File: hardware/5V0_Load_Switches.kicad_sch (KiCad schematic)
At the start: 28 parts, among them Q18 SI2302DDS-T1-GE3, Q19 SI2302DDS-T1-GE3, Q20 SI2302DDS-T1-GE3, U1 LMV321RIYLT, U10 INA199C3DCKR, U4 INA199C1DCKR, U5 NVTFS5116PLTAG, U6 NVTFS5116PLTAG, U7 NVTFS5116PLTAG, U9 INA199C3DCKR

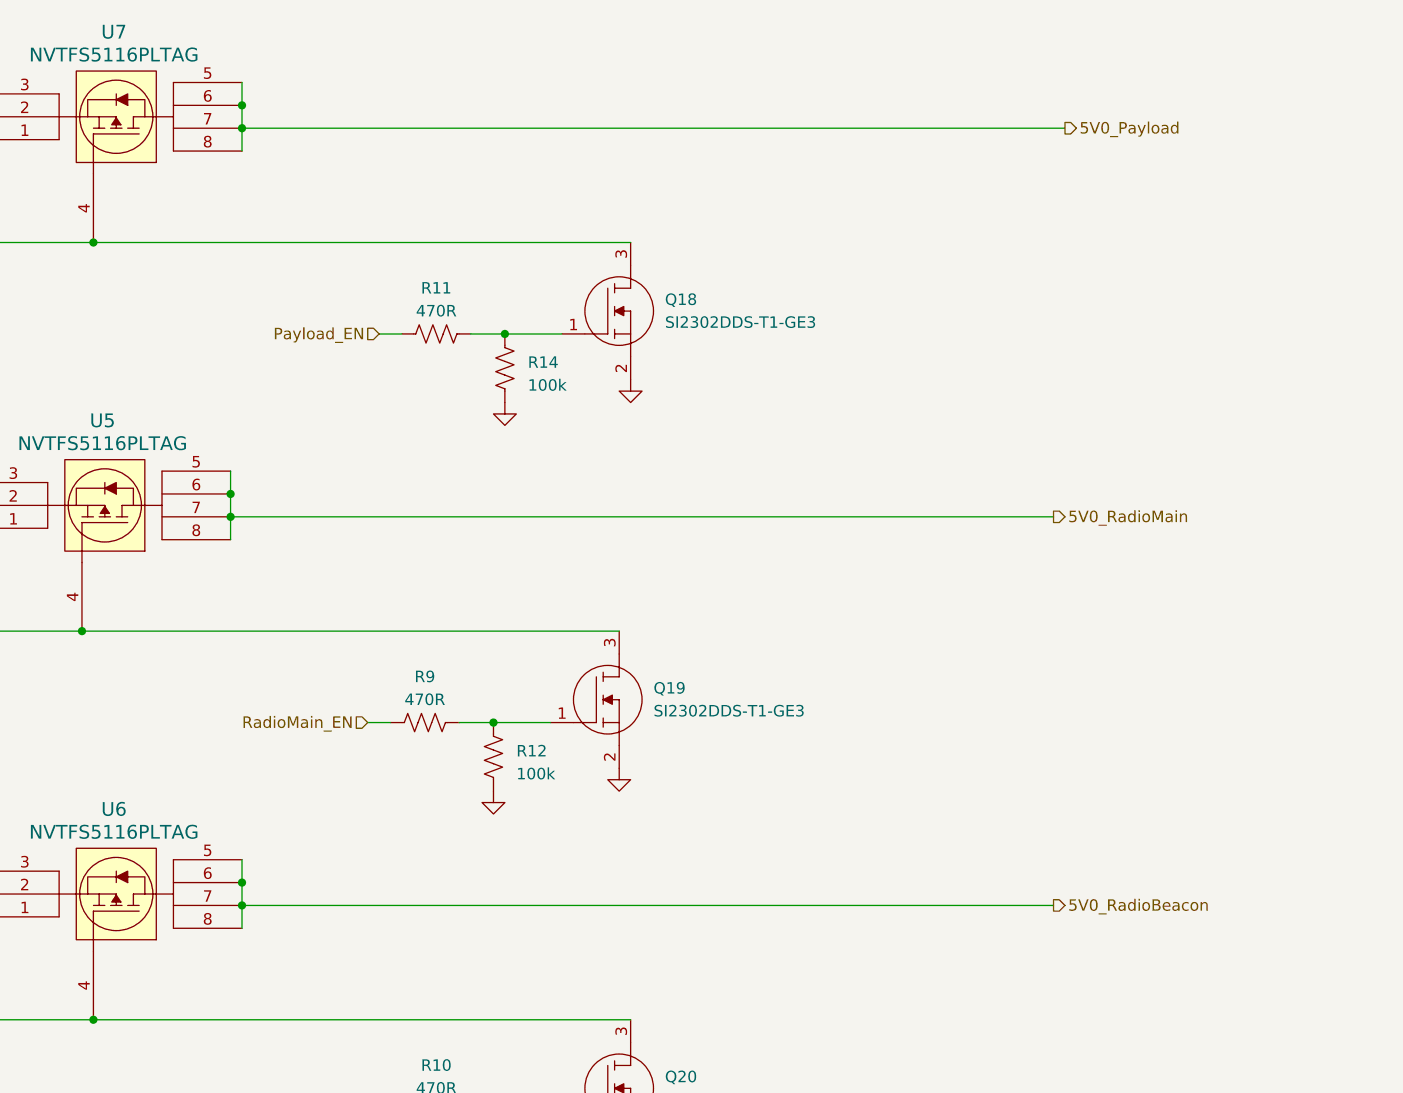
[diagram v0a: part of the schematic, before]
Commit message: hardware: Adding some 3D models, changing the placement of components and routing more nets.
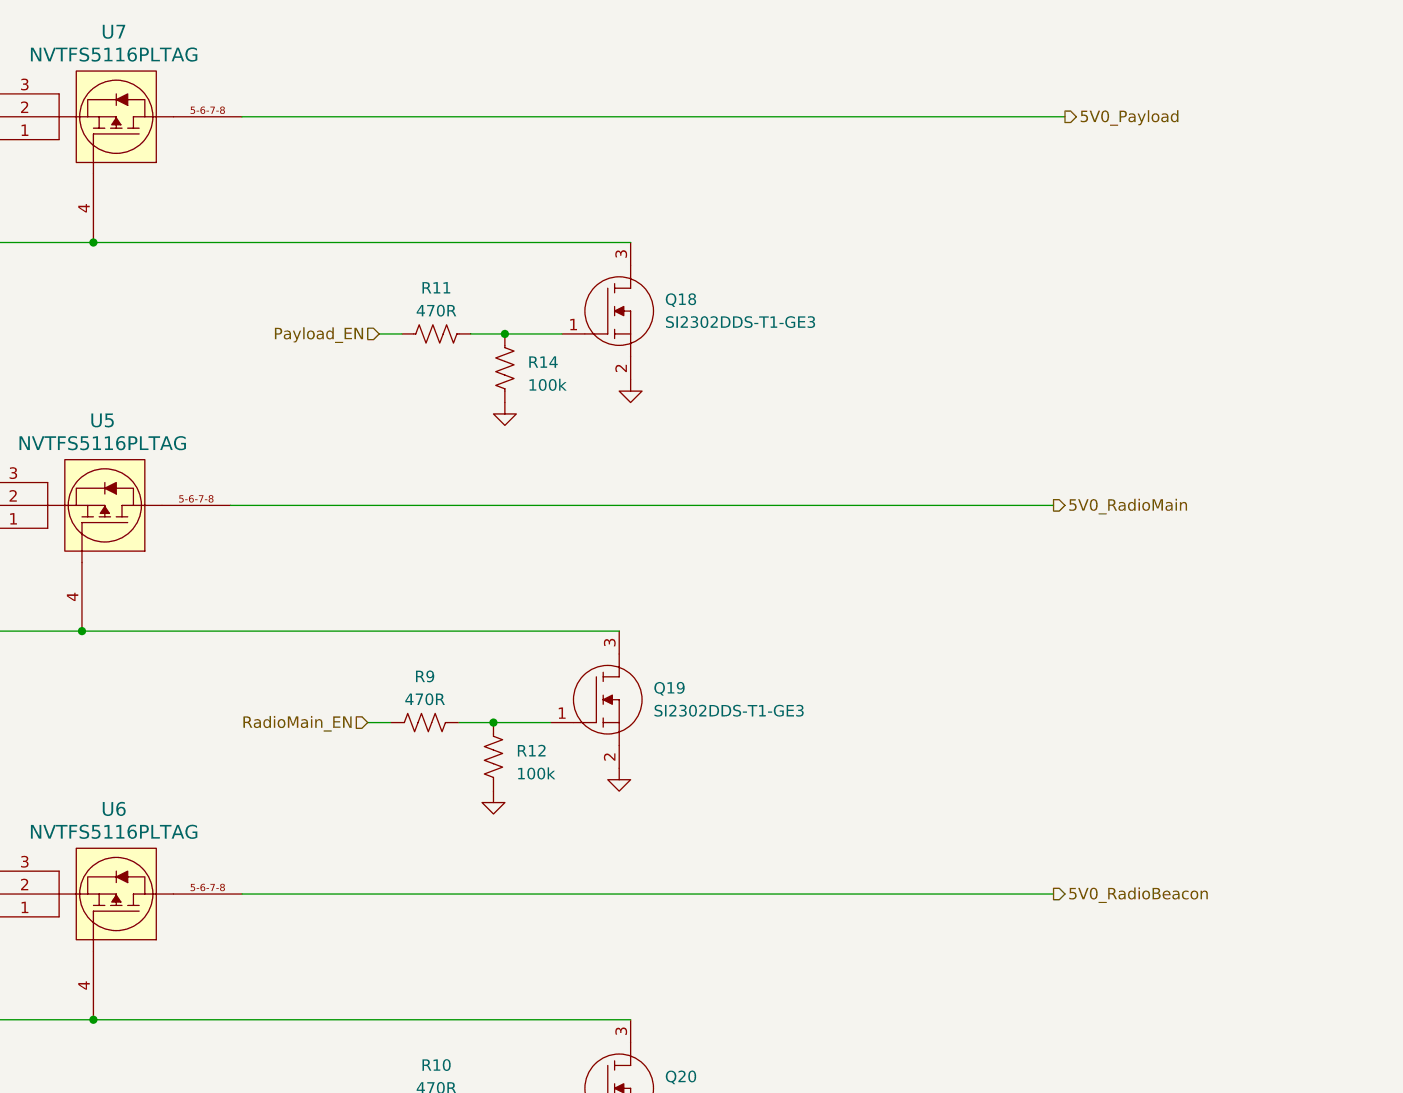
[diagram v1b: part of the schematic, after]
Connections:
- net 5V0_Payload: now also U7.5-6-7-8; no longer U7.5, U7.6, U7.7, U7.8
- net 5V0_RadioBeacon: now also U6.5-6-7-8; no longer U6.5, U6.6, U6.7, U6.8
- net 5V0_RadioMain: now also U5.5-6-7-8; no longer U5.5, U5.6, U5.7, U5.8
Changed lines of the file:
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@@
   (junction (at 66.04 99.06) (diameter 0) (color 0 0 0 0)
   )
-  (junction (at 148.59 71.12) (diameter 0) (color 0 0 0 0)
-  )
   (junction (at 22.86 115.57) (diameter 0) (color 0 0 0 0)
   )
   (junction (at 121.92 115.57) (diameter 0) (color 0 0 0 0)
   )
-  (junction (at 148.59 73.66) (diameter 0) (color 0 0 0 0)
-  )
   (junction (at 66.04 142.24) (diameter 0) (color 0 0 0 0)
   )
@@
   (junction (at 57.15 125.73) (diameter 0) (color 0 0 0 0)
   )
-  (junction (at 149.86 114.3) (diameter 0) (color 0 0 0 0)
-  )
   (junction (at 133.35 43.18) (diameter 0) (color 0 0 0 0)
   )
-  (junction (at 149.86 30.48) (diameter 0) (color 0 0 0 0)
-  )
   (junction (at 260.35 162.56) (diameter 0) (color 0 0 0 0)
   )
@@
   (junction (at 57.15 93.98) (diameter 0) (color 0 0 0 0)
   )
-  (junction (at 149.86 116.84) (diameter 0) (color 0 0 0 0)
-  )
   (junction (at 57.15 72.39) (diameter 0) (color 0 0 0 0)
   )
@@
   (junction (at 105.41 29.21) (diameter 0) (color 0 0 0 0)
   )
-  (junction (at 149.86 27.94) (diameter 0) (color 0 0 0 0)
-  )
   (junction (at 57.15 86.36) (diameter 0) (color 0 0 0 0)
   )
@@
     (stroke (width 0) (type default))
   )
-  (wire (pts (xy 149.86 27.94) (xy 149.86 30.48))
-    (stroke (width 0) (type default))
-  )
   (wire (pts (xy 76.2 72.39) (xy 104.14 72.39))
     (stroke (width 0) (type default))
@@
     (stroke (width 0) (type default))
   )
-  (wire (pts (xy 149.86 30.48) (xy 149.86 33.02))
-    (stroke (width 0) (type default))
-  )
   (wire (pts (xy 257.81 152.4) (xy 250.19 152.4))
     (stroke (width 0) (type default))
@@
     (stroke (width 0) (type default))
   )
-  (wire (pts (xy 149.86 111.76) (xy 149.86 114.3))
-    (stroke (width 0) (type default))
-  )
   (wire (pts (xy 105.41 129.54) (xy 133.35 129.54))
     (stroke (width 0) (type default))
   )
-  (wire (pts (xy 149.86 116.84) (xy 240.03 116.84))
+  (wire (pts (xy 149.86 115.57) (xy 240.03 115.57))
     (stroke (width 0) (type default))
   )
@@
     (stroke (width 0) (type default))
   )
-  (wire (pts (xy 148.59 68.58) (xy 148.59 71.12))
-    (stroke (width 0) (type default))
-  )
   (wire (pts (xy 167.64 139.7) (xy 165.1 139.7))
     (stroke (width 0) (type default))
@@
   )
   (wire (pts (xy 166.37 96.52) (xy 163.83 96.52))
-    (stroke (width 0) (type default))
-  )
-  (wire (pts (xy 148.59 73.66) (xy 148.59 76.2))
     (stroke (width 0) (type default))
   )
@@
     (stroke (width 0) (type default))
   )
-  (wire (pts (xy 149.86 114.3) (xy 149.86 116.84))
-    (stroke (width 0) (type default))
-  )
   (wire (pts (xy 179.07 53.34) (xy 185.42 53.34))
     (stroke (width 0) (type default))
@@
     (stroke (width 0) (type default))
   )
-  (wire (pts (xy 149.86 30.48) (xy 241.3 30.48))
+  (wire (pts (xy 149.86 29.21) (xy 241.3 29.21))
     (stroke (width 0) (type default))
   )
@@
   )
   (wire (pts (xy 121.92 26.67) (xy 121.92 29.21))
-    (stroke (width 0) (type default))
-  )
-  (wire (pts (xy 149.86 25.4) (xy 149.86 27.94))
     (stroke (width 0) (type default))
   )
@@
     (stroke (width 0) (type default))
   )
-  (wire (pts (xy 149.86 116.84) (xy 149.86 119.38))
-    (stroke (width 0) (type default))
-  )
   (wire (pts (xy 121.92 115.57) (xy 121.92 118.11))
     (stroke (width 0) (type default))
@@
   )
   (wire (pts (xy 71.12 29.21) (xy 76.2 29.21))
-    (stroke (width 0) (type default))
-  )
-  (wire (pts (xy 148.59 71.12) (xy 148.59 73.66))
     (stroke (width 0) (type default))
   )
@@
     (stroke (width 1) (type default))
   )
-  (wire (pts (xy 148.59 73.66) (xy 240.03 73.66))
+  (wire (pts (xy 148.59 72.39) (xy 240.03 72.39))
     (stroke (width 0) (type default))
   )
@@
     (effects (font (size 1.27 1.27)) (justify right))
   )
-  (hierarchical_label "5V0_RadioMain" (shape output) (at 240.03 73.66 0) (fields_autoplaced)
+  (hierarchical_label "5V0_RadioMain" (shape output) (at 240.03 72.39 0) (fields_autoplaced)
     (effects (font (size 1.27 1.27)) (justify left))
   )
-  (hierarchical_label "5V0_Payload" (shape output) (at 241.3 30.48 0) (fields_autoplaced)
+  (hierarchical_label "5V0_Payload" (shape output) (at 241.3 29.21 0) (fields_autoplaced)
     (effects (font (size 1.27 1.27)) (justify left))
   )
@@
     (effects (font (size 1.27 1.27)) (justify right))
   )
-  (hierarchical_label "5V0_RadioBeacon" (shape output) (at 240.03 116.84 0) (fields_autoplaced)
+  (hierarchical_label "5V0_RadioBeacon" (shape output) (at 240.03 115.57 0) (fields_autoplaced)
     (effects (font (size 1.27 1.27)) (justify left))
   )
@@
     (pin "3")
     (pin "4")
-    (pin "5")
-    (pin "6")
-    (pin "7")
-    (pin "8")
+    (pin "5-6-7-8")
     (instances
       (project "eps-re_project"
@@
     (pin "3")
     (pin "4")
-    (pin "5")
-    (pin "6")
-    (pin "7")
-    (pin "8")
+    (pin "5-6-7-8")
     (instances
       (project "eps-re_project"
@@
     (pin "3")
     (pin "4")
-    (pin "5")
-    (pin "6")
-    (pin "7")
-    (pin "8")
+    (pin "5-6-7-8")
     (instances
       (project "eps-re_project"

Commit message: hardware: Updating schematics and layout.
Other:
- note added: "Output current ≤ 2A"
- note added: "Output current ≤ 600mA"
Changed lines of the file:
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@@
     (date "2023-08-03")
     (rev "v0.0")
-    (comment 1 "João C. E. Barcellos <joaoclaudiobarcellos@gmail.com>")
-    (comment 2 "Laura Debastiani <laudebastiani@gmail.com>")
+    (comment 1 "Davi Figueiredo <figueiredo.davi7@gmail.com> ")
+    (comment 2 "João C. E. Barcellos <joaoclaudiobarcellos@gmail.com>")
+    (comment 3 "Laura Debastiani <laudebastiani@gmail.com>")
   )
   (junction (at 57.15 43.18) (diameter 0) (color 0 0 0 0)
@@
   )
   (wire (pts (xy 76.2 72.39) (xy 104.14 72.39))
-    (stroke (width 0) (type default))
+    (stroke (width 1) (type default))
   )
   (wire (pts (xy 57.15 29.21) (xy 63.5 29.21))
-    (stroke (width 0) (type default))
+    (stroke (width 1) (type default))
   )
   (wire (pts (xy 57.15 29.21) (xy 57.15 39.37))
@@
   )
   (wire (pts (xy 22.86 72.39) (xy 57.15 72.39))
-    (stroke (width 0) (type default))
+    (stroke (width 1) (type default))
   )
   (wire (pts (xy 71.12 115.57) (xy 76.2 115.57))
-    (stroke (width 0) (type default))
+    (stroke (width 1) (type default))
   )
   (wire (pts (xy 257.81 152.4) (xy 250.19 152.4))
@@
   )
   (wire (pts (xy 149.86 115.57) (xy 240.03 115.57))
-    (stroke (width 0) (type default))
+    (stroke (width 1) (type default))
   )
   (wire (pts (xy 66.04 142.24) (xy 57.15 142.24))
@@
   )
   (wire (pts (xy 71.12 72.39) (xy 76.2 72.39))
-    (stroke (width 0) (type default))
+    (stroke (width 1) (type default))
   )
   (wire (pts (xy 104.14 72.39) (xy 104.14 78.74))
@@
   )
   (wire (pts (xy 22.86 29.21) (xy 57.15 29.21))
-    (stroke (width 0) (type default))
+    (stroke (width 1) (type default))
   )
   (wire (pts (xy 57.15 91.44) (xy 57.15 93.98))
@@
   )
   (wire (pts (xy 22.86 72.39) (xy 22.86 115.57))
-    (stroke (width 0) (type default))
+    (stroke (width 1) (type default))
   )
   (wire (pts (xy 121.92 113.03) (xy 121.92 115.57))
-    (stroke (width 0) (type default))
+    (stroke (width 1) (type default))
   )
   (wire (pts (xy 57.15 134.62) (xy 57.15 137.16))
@@
   )
   (wire (pts (xy 19.05 29.21) (xy 22.86 29.21))
-    (stroke (width 0) (type default))
+    (stroke (width 1) (type default))
   )
   (wire (pts (xy 260.35 162.56) (xy 270.51 162.56))
@@
   )
   (wire (pts (xy 121.92 29.21) (xy 121.92 31.75))
-    (stroke (width 0) (type default))
+    (stroke (width 1) (type default))
   )
   (wire (pts (xy 179.07 53.34) (xy 185.42 53.34))
@@
   )
   (wire (pts (xy 104.14 72.39) (xy 120.65 72.39))
-    (stroke (width 0) (type default))
+    (stroke (width 1) (type default))
   )
   (wire (pts (xy 149.86 29.21) (xy 241.3 29.21))
-    (stroke (width 0) (type default))
+    (stroke (width 1) (type default))
   )
   (wire (pts (xy 81.28 172.72) (xy 81.28 180.34))
@@
   )
   (wire (pts (xy 121.92 26.67) (xy 121.92 29.21))
-    (stroke (width 0) (type default))
+    (stroke (width 1) (type default))
   )
   (wire (pts (xy 120.65 72.39) (xy 120.65 74.93))
-    (stroke (width 0) (type default))
+    (stroke (width 1) (type default))
   )
   (wire (pts (xy 57.15 93.98) (xy 57.15 99.06))
@@
   )
   (wire (pts (xy 76.2 115.57) (xy 105.41 115.57))
-    (stroke (width 0) (type default))
+    (stroke (width 1) (type default))
   )
   (wire (pts (xy 76.2 55.88) (xy 76.2 50.8))
@@
   )
   (wire (pts (xy 120.65 69.85) (xy 120.65 72.39))
-    (stroke (width 0) (type default))
+    (stroke (width 1) (type default))
   )
   (wire (pts (xy 121.92 115.57) (xy 121.92 118.11))
-    (stroke (width 0) (type default))
+    (stroke (width 1) (type default))
   )
   (wire (pts (xy 66.04 55.88) (xy 57.15 55.88))
@@
   )
   (wire (pts (xy 57.15 115.57) (xy 63.5 115.57))
-    (stroke (width 0) (type default))
+    (stroke (width 1) (type default))
   )
   (wire (pts (xy 175.26 139.7) (xy 179.07 139.7))
@@
   )
   (wire (pts (xy 76.2 29.21) (xy 105.41 29.21))
-    (stroke (width 0) (type default))
+    (stroke (width 1) (type default))
   )
   (wire (pts (xy 22.86 115.57) (xy 22.86 156.21))
@@
   )
   (wire (pts (xy 57.15 72.39) (xy 63.5 72.39))
-    (stroke (width 0) (type default))
+    (stroke (width 1) (type default))
   )
   (wire (pts (xy 76.2 99.06) (xy 76.2 93.98))
@@
   )
   (wire (pts (xy 22.86 29.21) (xy 22.86 72.39))
-    (stroke (width 0) (type default))
+    (stroke (width 1) (type default))
   )
   (wire (pts (xy 179.07 139.7) (xy 185.42 139.7))
@@
   )
   (wire (pts (xy 71.12 29.21) (xy 76.2 29.21))
-    (stroke (width 0) (type default))
+    (stroke (width 1) (type default))
   )
   (bus (pts (xy 260.35 142.24) (xy 260.35 146.05))
@@
   )
   (wire (pts (xy 148.59 72.39) (xy 240.03 72.39))
-    (stroke (width 0) (type default))
+    (stroke (width 1) (type default))
   )
   (wire (pts (xy 105.41 29.21) (xy 121.92 29.21))
-    (stroke (width 0) (type default))
+    (stroke (width 1) (type default))
   )
   (wire (pts (xy 22.86 168.91) (xy 40.64 168.91))
@@
   )
   (wire (pts (xy 22.86 115.57) (xy 57.15 115.57))
-    (stroke (width 0) (type default))
+    (stroke (width 1) (type default))
   )
   (wire (pts (xy 105.41 115.57) (xy 121.92 115.57))
-    (stroke (width 0) (type default))
+    (stroke (width 1) (type default))
+  )
+  (text "Output current ≤ 600mA" (at 212.09 71.12 0)
+    (effects (font (size 1.27 1.27)) (justify left bottom))
+  )
+  (text "Output current ≤ 600mA" (at 212.09 114.3 0)
+    (effects (font (size 1.27 1.27)) (justify left bottom))
+  )
+  (text "Output current ≤ 2A" (at 212.09 27.94 0)
+    (effects (font (size 1.27 1.27)) (justify left bottom))
   )
   (label "AMUX8" (at 250.19 152.4 180) (fields_autoplaced)
